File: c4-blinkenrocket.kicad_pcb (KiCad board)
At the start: 2 copper layers, 47 x 96.3 mm, 12 parts, among them J1 ISP, U1 ATtiny88-AU

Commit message: A first complete Version of the Blinkenrocket
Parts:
- removed the R2 at (119.1, 126.5)
- added C3: 470 nF, Capacitor_SMD:C_1206_3216Metric_Pad1.42x1.75mm_HandSolder, B.Cu at (125.0, 103.0)
- added H2: MountingHole, MountingHole:MountingHole_3.2mm_M3_Pad, F.Cu at (108.2, 141.8)
- added H3: MountingHole, MountingHole:MountingHole_3.2mm_M3_Pad, F.Cu at (142.0, 141.8)
- added JP1: SJ1-3523N, footprints:Jack_3.5mm_CUI_SJ1-3523N_Horizontal, F.Cu at (125.0, 127.0)
- added JP3: Conn_01x04, Connector_PinHeader_2.54mm:PinHeader_1x04_P2.54mm_Vertical, F.Cu at (144.0, 85.5)
- added JP4: Conn_01x04, Connector_PinHeader_2.54mm:PinHeader_1x04_P2.54mm_Vertical, F.Cu at (106.0, 85.5)
- added LED1: LED_Matrix_8x8, footprints:LED_KWM-30881XVB_8x8_3mm_3.2x3.2mm, F.Cu at (125.0, 89.0)
- added R3: 16, Resistor_SMD:R_1206_3216Metric_Pad1.42x1.75mm_HandSolder, B.Cu at (114.0, 127.0)
- added R4: 10k, Resistor_SMD:R_1206_3216Metric_Pad1.42x1.75mm_HandSolder, B.Cu at (136.0, 117.0)
- added R5: 10k, Resistor_SMD:R_1206_3216Metric_Pad1.42x1.75mm_HandSolder, B.Cu at (130.0, 117.0)
- added SW1: SW_SPST, Button_Switch_THT:SW_PUSH_6mm_H5mm, F.Cu at (104.5, 132.0)
- added SW2: SW_SPST, Button_Switch_THT:SW_PUSH_6mm_H5mm, F.Cu at (139.0, 132.0)
- added U2: 24CW640-I_SN, Package_SO:SOIC-8_3.9x4.9mm_P1.27mm, B.Cu at (139.0, 123.0)
- C1, C2: footprint Capacitor_SMD:C_1206_3216Metric -> Capacitor_SMD:C_1206_3216Metric_Pad1.42x1.75mm_HandSolder
- H1: footprint MountingHole:MountingHole_3.2mm_M3 -> MountingHole:MountingHole_3.2mm_M3_Pad
- R1: footprint Resistor_SMD:R_1206_3216Metric -> Resistor_SMD:R_1206_3216Metric_Pad1.42x1.75mm_HandSolder
- R2: renamed from R3; footprint Resistor_SMD:R_1206_3216Metric -> Resistor_SMD:R_1206_3216Metric_Pad1.42x1.75mm_HandSolder
- R6: renamed from R4; footprint Resistor_SMD:R_1206_3216Metric -> Resistor_SMD:R_1206_3216Metric_Pad1.42x1.75mm_HandSolder
- moved R1 20.2 mm to (114.0, 103.0)
- moved C1 15.5 mm to (114.0, 111.0)
- moved R2 12.8 mm to (114.0, 107.0), turned to 180 degrees
- moved D1 9.70 mm to (114.0, 119.0)
- moved C2 7.88 mm to (114.0, 115.0), turned to 180 degrees
- moved D2 6.18 mm to (114.0, 123.0)
- moved BT1 5.00 mm to (125.0, 70.0)
- moved J1 2.00 mm to (122.5, 112.0)
- moved R6 1.58 mm to (124.0, 117.0)
- moved U1 1.00 mm to (125.0, 94.0), turned to 90 degrees
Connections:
- net /SCK renamed /R6
- U1 pad 1: Net-(U1-Pad1) -> /C4
- U1 pad 10: Net-(U1-Pad10) -> /C7
- U1 pad 11: Net-(U1-Pad11) -> /C8
- U1 pad 12: Net-(U1-Pad12) -> /R1
- U1 pad 13: Net-(U1-Pad13) -> /R2
- U1 pad 14: Net-(U1-Pad14) -> /R3
- U1 pad 2: Net-(U1-Pad2) -> /C5
- U1 pad 20: Net-(U1-Pad20) -> /B1
- U1 pad 22: Net-(U1-Pad22) -> /E4
- U1 pad 23: Net-(U1-Pad23) -> /E1
- U1 pad 24: Net-(U1-Pad24) -> /E2
- U1 pad 25: Net-(U1-Pad25) -> /E3
- U1 pad 26: Net-(U1-Pad26) -> /B2
- U1 pad 27: Net-(U1-Pad27) -> /SDA
- U1 pad 28: Net-(U1-Pad28) -> /SCL
- U1 pad 3: Net-(U1-Pad3) -> (no net)
- U1 pad 30: Net-(U1-Pad30) -> /C1
- U1 pad 31: Net-(U1-Pad31) -> /C2
- U1 pad 32: Net-(U1-Pad32) -> /C3
- U1 pad 7: Net-(U1-Pad7) -> /R7
- U1 pad 8: Net-(U1-Pad8) -> /R8
- U1 pad 9: Net-(U1-Pad9) -> /C6
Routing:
- net VCC: track 0.00 -> 145.4 mm
- net /B1: track 0.00 -> 82.3 mm, vias 0 -> 1
- net /R6: track 0.00 -> 82.2 mm
- net /B2: track 0.00 -> 77.3 mm, vias 0 -> 1
- net /AVR_AUDIO_IN: track 0.00 -> 57.5 mm, vias 0 -> 2
- net /E3: track 0.00 -> 52.6 mm, vias 0 -> 1
- net /MOSI: track 0.00 -> 52.3 mm
- net /SCL: track 0.00 -> 49.6 mm, vias 0 -> 2
- net /SDA: track 0.00 -> 49.4 mm, vias 0 -> 2
- net /MISO: track 0.00 -> 44.4 mm, vias 0 -> 1
- net /R8: track 0.00 -> 43.1 mm, vias 0 -> 1
- net /E4: track 0.00 -> 42.9 mm, vias 0 -> 1
- net /C4: track 0.00 -> 40.2 mm, vias 0 -> 1
- net /R3: track 0.00 -> 40.1 mm
- net /RESET: track 0.00 -> 36.8 mm, vias 0 -> 1
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- added copper zone on B.Cu, net GND
- added copper zone on F.Cu, net GND
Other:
- board text added: "RZL"
- board text added: "Rev C4"
- board text added: "blinkenrocket.de"
- board text added: "chaosdorf"
- board text added: "metalab"
- board text added: "muzy"
- board text added: "overflo"
- board text added: "shackspace"

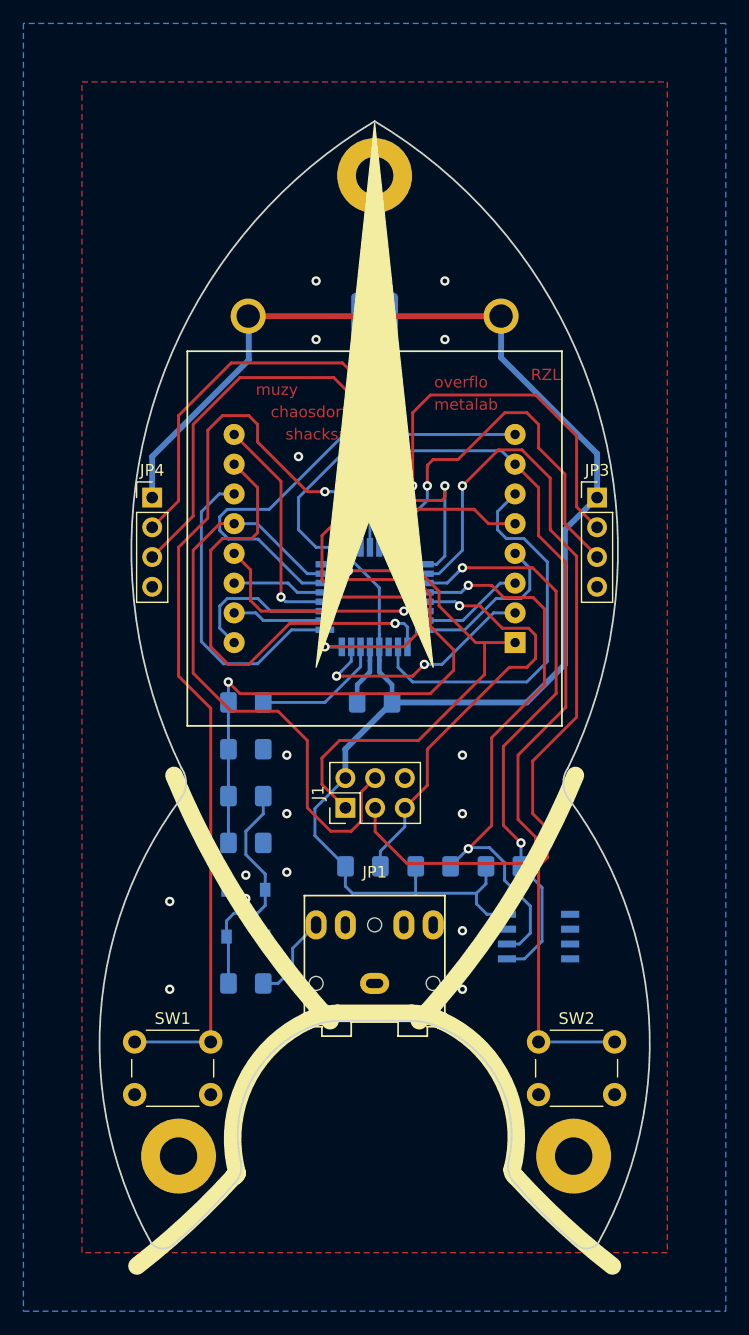
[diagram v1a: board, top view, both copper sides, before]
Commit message: Swapped battery holder, made footprints easier to solder
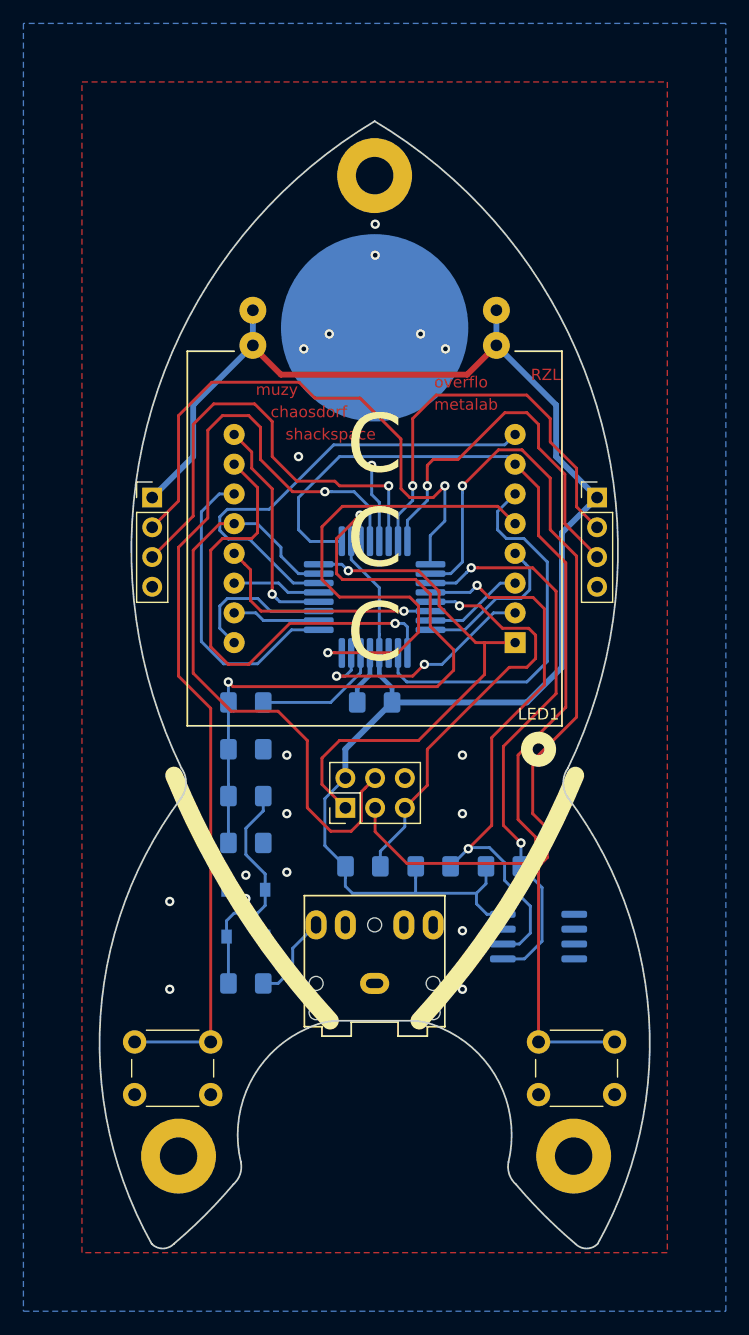
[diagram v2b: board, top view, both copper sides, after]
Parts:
- added G***: LOGO, footprints:explosion, B.Cu at (134.2, 109.2)
- added G***: LOGO, footprints:hexogen-platine-soldermask-smallest, F.Cu at (125.0, 67.9)
- BT1: value BK-913 -> BAT-HLD-001-THM; footprint footprints:BAT_BK-913_footprint -> footprints:BAT_Linx_BAT-HLD-001-THM
- U1: footprint Package_QFP:TQFP-32_7x7mm_P0.8mm -> footprints:TQFP-32_7x7mm_P0.8mm_Handsolder
- U2: footprint Package_SO:SOIC-8_3.9x4.9mm_P1.27mm -> footprints:SOIC-8_4.9x3.9mm_P1.27mm_Handsolder
- moved BT1 1.00 mm to (125.0, 71.0)
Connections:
- U2 pad 1: (no net) -> Net-(U2-Pad1)
- U2 pad 2: (no net) -> Net-(U2-Pad2)
- U2 pad 3: (no net) -> Net-(U2-Pad3)
- U2 pad 7: (no net) -> Net-(U2-Pad7)
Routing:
- net /E3: track 52.6 -> 48.7 mm
- net /E4: track 42.9 -> 40.1 mm
- net VCC: track 145.4 -> 147.4 mm
- net /B1: track 82.3 -> 83.6 mm
- net /AVR_AUDIO_IN: track 57.5 -> 58.4 mm
- net /E1: track 36.6 -> 35.9 mm
- net /B2: track 77.3 -> 77.9 mm
- net /R6: track 82.2 -> 81.6 mm
- net GND: vias 18 -> 19
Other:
- board text added: "C C C"
- board text added: "E1"
- board text added: "E2"
- board text added: "E3"
- board text added: "E4"
- board text added: "GND"
- board text added: "VCC"

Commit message: Fabrication data as ordered at the usual chinese pcb manufactures
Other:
- rule pad_to_mask_clearance: 0.051 -> 0.05
- rule solder_mask_min_width: 0.25 -> 0.15
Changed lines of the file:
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@@
     (thickness 1.6)
     (drawings 38)
-    (tracks 413)
+    (tracks 415)
     (zones 0)
     (modules 26)
@@
   )
   (setup
-    (last_trace_width 0.5)
+    (last_trace_width 0.25)
     (user_trace_width 0.25)
     (user_trace_width 0.4)
@@
     (pad_size 1.524 1.524)
     (pad_drill 0.762)
-    (pad_to_mask_clearance 0.051)
-    (solder_mask_min_width 0.25)
+    (pad_to_mask_clearance 0.05)
+    (solder_mask_min_width 0.15)
+    (pad_to_paste_clearance_ratio -0.1)
     (aux_axis_origin 100 150)
     (grid_origin 100 150)
     (visible_elements FFFFFF7F)
     (pcbplotparams
-      (layerselection 0x010fc_ffffffff)
-      (usegerberextensions false)
-      (usegerberattributes false)
+      (layerselection 0x010f4_ffffffff)
+      (usegerberextensions true)
+      (usegerberattributes true)
       (usegerberadvancedattributes false)
       (creategerberjobfile false)
-      (excludeedgelayer true)
-      (linewidth 0.100000)
+      (excludeedgelayer false)
+      (linewidth 0.150000)
       (plotframeref false)
       (viasonmask false)
       (mode 1)
-      (useauxorigin false)
+      (useauxorigin true)
       (hpglpennumber 1)
       (hpglpenspeed 20)
@@
       (outputformat 1)
       (mirror false)
-      (drillshape 1)
+      (drillshape 0)
       (scaleselection 1)
-      (outputdirectory ""))
+      (outputdirectory "fab/"))
   )
   (net 0 "")
@@
     (descr "Capacitor SMD 1206 (3216 Metric), square (rectangular) end terminal, IPC_7351 nominal with elongated pad for handsoldering. (Body size source: http://www.tortai-tech.com/upload/download/2011102023233369053.pdf), generated with kicad-footprint-generator")
     (tags "capacitor handsolder")
+    (solder_paste_margin -10)
     (attr smd)
     (fp_text reference C3 (at 0 1.82) (layer B.SilkS)
@@
     (descr "Resistor SMD 1206 (3216 Metric), square (rectangular) end terminal, IPC_7351 nominal with elongated pad for handsoldering. (Body size source: http://www.tortai-tech.com/upload/download/2011102023233369053.pdf), generated with kicad-footprint-generator")
     (tags "resistor handsolder")
+    (solder_paste_margin -10)
     (attr smd)
     (fp_text reference R6 (at 0 1.82) (layer B.SilkS)
@@
     (descr "Resistor SMD 1206 (3216 Metric), square (rectangular) end terminal, IPC_7351 nominal with elongated pad for handsoldering. (Body size source: http://www.tortai-tech.com/upload/download/2011102023233369053.pdf), generated with kicad-footprint-generator")
     (tags "resistor handsolder")
+    (solder_paste_margin -10)
     (attr smd)
     (fp_text reference R5 (at 0 -2 180) (layer B.SilkS)
@@
     (descr "Resistor SMD 1206 (3216 Metric), square (rectangular) end terminal, IPC_7351 nominal with elongated pad for handsoldering. (Body size source: http://www.tortai-tech.com/upload/download/2011102023233369053.pdf), generated with kicad-footprint-generator")
     (tags "resistor handsolder")
+    (solder_paste_margin -10)
     (attr smd)
     (fp_text reference R4 (at 0 -2 180) (layer B.SilkS)
@@
     (descr "Resistor SMD 1206 (3216 Metric), square (rectangular) end terminal, IPC_7351 nominal with elongated pad for handsoldering. (Body size source: http://www.tortai-tech.com/upload/download/2011102023233369053.pdf), generated with kicad-footprint-generator")
     (tags "resistor handsolder")
+    (solder_paste_margin -10)
     (attr smd)
     (fp_text reference R3 (at 0 1.9) (layer B.SilkS)
@@
     (descr "Resistor SMD 1206 (3216 Metric), square (rectangular) end terminal, IPC_7351 nominal with elongated pad for handsoldering. (Body size source: http://www.tortai-tech.com/upload/download/2011102023233369053.pdf), generated with kicad-footprint-generator")
     (tags "resistor handsolder")
+    (solder_paste_margin -10)
     (attr smd)
     (fp_text reference R2 (at 0 -2 180) (layer B.SilkS)
@@
     (descr "Resistor SMD 1206 (3216 Metric), square (rectangular) end terminal, IPC_7351 nominal with elongated pad for handsoldering. (Body size source: http://www.tortai-tech.com/upload/download/2011102023233369053.pdf), generated with kicad-footprint-generator")
     (tags "resistor handsolder")
+    (solder_paste_margin -10)
     (attr smd)
     (fp_text reference R1 (at 0 2) (layer B.SilkS)
@@
     (descr "Capacitor SMD 1206 (3216 Metric), square (rectangular) end terminal, IPC_7351 nominal with elongated pad for handsoldering. (Body size source: http://www.tortai-tech.com/upload/download/2011102023233369053.pdf), generated with kicad-footprint-generator")
     (tags "capacitor handsolder")
+    (solder_paste_margin -10)
     (attr smd)
     (fp_text reference C2 (at 0 -2 180) (layer B.SilkS)
@@
     (descr "Capacitor SMD 1206 (3216 Metric), square (rectangular) end terminal, IPC_7351 nominal with elongated pad for handsoldering. (Body size source: http://www.tortai-tech.com/upload/download/2011102023233369053.pdf), generated with kicad-footprint-generator")
     (tags "capacitor handsolder")
+    (solder_paste_margin -10)
     (attr smd)
     (fp_text reference C1 (at 0 1.82) (layer B.SilkS)
@@
     (descr SOD-123)
     (tags SOD-123)
+    (solder_paste_margin -10)
     (attr smd)
     (fp_text reference D2 (at 0 2) (layer B.SilkS)
@@
     (descr SOD-123)
     (tags SOD-123)
+    (solder_paste_margin -10)
     (attr smd)
     (fp_text reference D1 (at 0 2) (layer B.SilkS)
@@
   (segment (start 126.4875 103) (end 126.4875 101.7375) (width 0.4) (layer B.Cu) (net 3))
   (segment (start 126.4875 101.7375) (end 125.4 100.65) (width 0.4) (layer B.Cu) (net 3))
-  (segment (start 120.75 111.21) (end 122.5 109.46) (width 0.25) (layer B.Cu) (net 3))
-  (segment (start 122.5125 117) (end 120.75 115.2375) (width 0.25) (layer B.Cu) (net 3))
-  (segment (start 120.75 115.2375) (end 120.75 111.21) (width 0.25) (layer B.Cu) (net 3))
   (segment (start 114.6 72.5) (end 114.6 69.5) (width 0.5) (layer B.Cu) (net 3))
   (segment (start 109.6 77.5) (end 114.6 72.5) (width 0.5) (layer B.Cu) (net 3))
@@
   (segment (start 114.6 72.5) (end 114.6 72.6) (width 0.5) (layer F.Cu) (net 3))
   (segment (start 114.6 72.6) (end 117 75) (width 0.5) (layer F.Cu) (net 3))
+  (segment (start 120.75 111.21) (end 122.5 109.46) (width 0.25) (layer B.Cu) (net 3))
+  (segment (start 120.75 115.05) (end 120.75 111.21) (width 0.25) (layer B.Cu) (net 3))
+  (segment (start 122.5125 117) (end 122.5125 116.8125) (width 0.25) (layer B.Cu) (net 3))
+  (segment (start 122.5125 116.8125) (end 120.75 115.05) (width 0.25) (layer B.Cu) (net 3))
   (segment (start 112.5125 114.025) (end 112.5125 111) (width 0.25) (layer B.Cu) (net 4))
   (segment (start 112.5125 115) (end 112.5125 114.025) (width 0.25) (layer B.Cu) (net 4))
@@
   (segment (start 111.774999 94.761999) (end 112.411999 94.124999) (width 0.25) (layer B.Cu) (net 33))
   (segment (start 115.024999 94.124999) (end 116.1 95.2) (width 0.25) (layer B.Cu) (net 33))
-  (segment (start 137.365 123.635) (end 136.3 123.635) (width 0.25) (layer B.Cu) (net 34))
-  (segment (start 138.3 122.7) (end 137.365 123.635) (width 0.25) (layer B.Cu) (net 34))
-  (segment (start 138.3 120.4) (end 138.3 122.7) (width 0.25) (layer B.Cu) (net 34))
-  (segment (start 133.0875 115.4) (end 134.81319 115.4) (width 0.25) (layer B.Cu) (net 34))
-  (segment (start 131.4875 117) (end 133.0875 115.4) (width 0.25) (layer B.Cu) (net 34))
-  (segment (start 136.1 116.68681) (end 136.1 118.2) (width 0.25) (layer B.Cu) (net 34))
-  (segment (start 134.81319 115.4) (end 136.1 116.68681) (width 0.25) (layer B.Cu) (net 34))
-  (segment (start 136.1 118.2) (end 138.3 120.4) (width 0.25) (layer B.Cu) (net 34))
   (via (at 133 115.5) (size 0.8) (drill 0.4) (layers F.Cu B.Cu) (net 34))
   (segment (start 134.785001 94.035001) (end 134.149999 93.399999) (width 0.25) (layer F.Cu) (net 34))
@@
   (segment (start 139.5 101.5) (end 139.5 95) (width 0.25) (layer F.Cu) (net 34))
   (segment (start 133.350001 93.399999) (end 133.75 93) (width 0.25) (layer B.Cu) (net 34))
+  (segment (start 137.365 123.635) (end 136.3 123.635) (width 0.25) (layer B.Cu) (net 34))
+  (segment (start 136.1 118.2) (end 138.3 120.4) (width 0.25) (layer B.Cu) (net 34))
+  (segment (start 131.4875 117) (end 131.4875 116.8125) (width 0.25) (layer B.Cu) (net 34))
+  (segment (start 131.4875 116.8125) (end 132.9 115.4) (width 0.25) (layer B.Cu) (net 34))
+  (segment (start 132.9 115.4) (end 135.1 115.4) (width 0.25) (layer B.Cu) (net 34))
+  (segment (start 135.1 115.4) (end 136.1 116.4) (width 0.25) (layer B.Cu) (net 34))
+  (segment (start 138.3 122.7) (end 137.365 123.635) (width 0.25) (layer B.Cu) (net 34))
+  (segment (start 138.3 120.4) (end 138.3 122.7) (width 0.25) (layer B.Cu) (net 34))
+  (segment (start 136.1 116.4) (end 136.1 118.2) (width 0.25) (layer B.Cu) (net 34))
   (segment (start 139.3 118.8125) (end 137.4875 117) (width 0.25) (layer B.Cu) (net 35))
   (segment (start 139.3 123.4) (end 139.3 118.8125) (width 0.25) (layer B.Cu) (net 35))
